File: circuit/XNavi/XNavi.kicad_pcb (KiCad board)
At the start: 2 copper layers, 60 x 60 mm, 34 parts, among them J1 Micro_SD_Card_Det, J2 Conn_01x06, J3 Conn_01x04, J4 Conn_01x06, J5 Conn_01x02, J6 Conn_Coaxial, J7 Conn_01x04, U1 STM32G441KBTx, U3 ASM330LHHTR, U4 MAX-M10S, U5 MAX3485

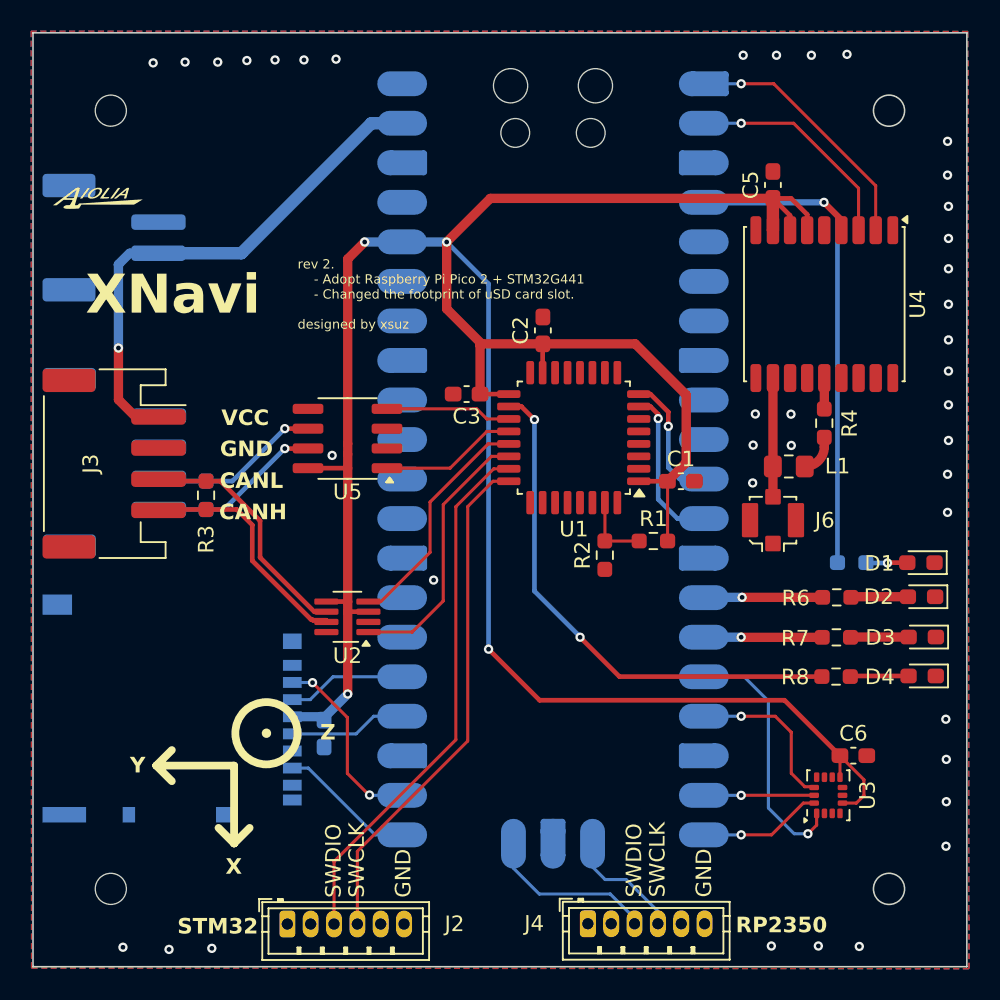
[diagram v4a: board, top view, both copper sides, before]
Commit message: UARTの信号線変更,基板を発注
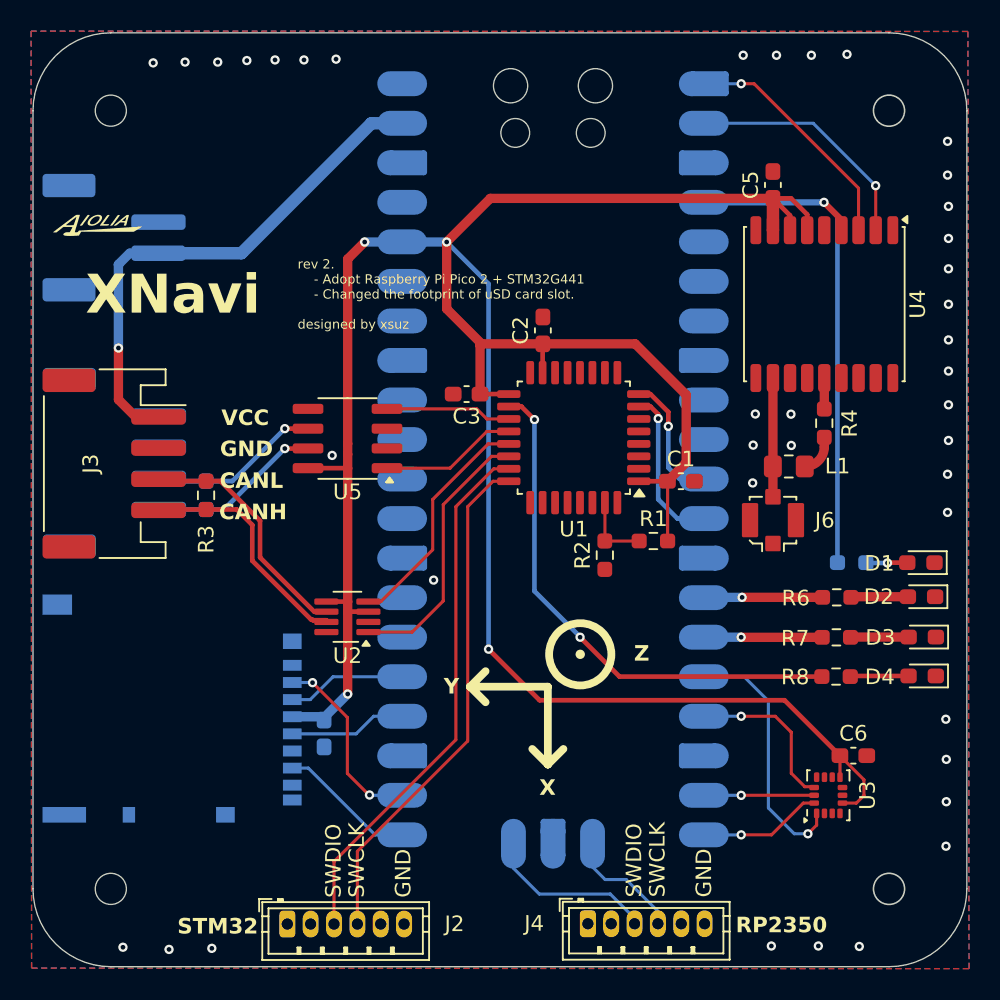
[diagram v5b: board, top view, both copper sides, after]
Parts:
- moved G*** 1.74 mm to (24.1, 32.5)
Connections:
- U4 pad 2: TX1 -> RX1
- U4 pad 3: RX1 -> TX1
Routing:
- net TX1: track 16.6 -> 15.4 mm
- net RX1: track 14.4 -> 15.6 mm
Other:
- outline, holes or cut-outs redrawn
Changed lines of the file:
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@@
 			(outputformat 1)
 			(mirror no)
-			(drillshape 1)
+			(drillshape 0)
 			(scaleselection 1)
-			(outputdirectory "")
+			(outputdirectory "out")
 		)
 	)
@@
 			(layers "F.Cu" "F.Mask" "F.Paste")
 			(roundrect_rratio 0.25)
-			(net 44 "TX1")
+			(net 35 "RX1")
 			(pinfunction "TXD")
 			(pintype "output")
@@
 			(layers "F.Cu" "F.Mask" "F.Paste")
 			(roundrect_rratio 0.25)
-			(net 35 "RX1")
+			(net 44 "TX1")
 			(pinfunction "RXD")
 			(pintype "input")
@@
 	(footprint "AIOLIA:AIOLIA"
 		(layer "F.Cu")
-		(at 24.133585 30.715897 -30)
+		(at 24.123585 32.455897 -30)
 		(property "Reference" "G***"
 			(at 0 0 150)
@@
 	)
 	(gr_circle
-		(center 35 65)
-		(end 35.25 65)
+		(center 55.16 59.93)
+		(end 55.41 59.93)
 		(stroke
 			(width 0.1)
@@
 	)
 	(gr_circle
-		(center 35 65)
-		(end 37 65)
+		(center 55.16 59.93)
+		(end 57.16 59.93)
 		(stroke
 			(width 0.5)
@@
 	)
 	(gr_line
-		(start 27.92 67.08)
-		(end 28.92 66.08)
+		(start 48.08 62.01)
+		(end 49.08 61.01)
 		(stroke
 			(width 0.5)
@@
 	)
 	(gr_line
-		(start 32.92 72.08)
-		(end 33.92 71.08)
+		(start 53.08 67.01)
+		(end 54.08 66.01)
 		(stroke
 			(width 0.5)
@@
 	)
 	(gr_line
-		(start 32.92 67.08)
-		(end 32.92 72.08)
+		(start 53.08 62.01)
+		(end 53.08 67.01)
 		(stroke
 			(width 0.5)
@@
 	)
 	(gr_line
-		(start 32.92 67.08)
-		(end 27.92 67.08)
+		(start 53.08 62.01)
+		(end 48.08 62.01)
 		(stroke
 			(width 0.5)
@@
 	)
 	(gr_line
-		(start 32.92 72.08)
-		(end 31.92 71.08)
+		(start 53.08 67.01)
+		(end 52.08 66.01)
 		(stroke
 			(width 0.5)
@@
 	)
 	(gr_line
-		(start 27.92 67.08)
-		(end 28.92 68.08)
+		(start 48.08 62.01)
+		(end 49.08 63.01)
 		(stroke
 			(width 0.5)
@@
 		(layer "Dwgs.User")
 	)
-	(gr_rect
-		(start 20 20)
-		(end 80 80)
+	(gr_arc
+		(start 25 80)
+		(mid 21.464466 78.535534)
+		(end 20 75)
 		(stroke
-			(width 0.1)
+			(width 0.05)
 			(type solid)
 		)
-		(fill no)
 		(layer "Edge.Cuts")
 	)
@@
 		(layer "Edge.Cuts")
 	)
+	(gr_line
+		(start 75 20)
+		(end 25 20)
+		(stroke
+			(width 0.05)
+			(type default)
+		)
+		(layer "Edge.Cuts")
+	)
+	(gr_line
+		(start 20 25)
+		(end 20 75)
+		(stroke
+			(width 0.05)
+			(type default)
+		)
+		(layer "Edge.Cuts")
+	)
+	(gr_line
+		(start 25 80)
+		(end 75 80)
+		(stroke
+			(width 0.05)
+			(type default)
+		)
+		(layer "Edge.Cuts")
+	)
+	(gr_arc
+		(start 20 25)
+		(mid 21.464466 21.464466)
+		(end 25 20)
+		(stroke
+			(width 0.05)
+			(type solid)
+		)
+		(layer "Edge.Cuts")
+	)
+	(gr_arc
+		(start 80 75)
+		(mid 78.535534 78.535534)
+		(end 75 80)
+		(stroke
+			(width 0.05)
+			(type solid)
+		)
+		(layer "Edge.Cuts")
+	)
+	(gr_arc
+		(start 75 20)
+		(mid 78.535534 21.464466)
+		(end 80 25)
+		(stroke
+			(width 0.05)
+			(type solid)
+		)
+		(layer "Edge.Cuts")
+	)
 	(gr_circle
 		(center 75 75)
@@
 		(layer "Edge.Cuts")
 	)
+	(gr_line
+		(start 80 75)
+		(end 80 25)
+		(stroke
+			(width 0.05)
+			(type default)
+		)
+		(layer "Edge.Cuts")
+	)
 	(gr_text "Z"
-		(at 38.45 65.53 0)
+		(at 58.61 60.46 0)
 		(layer "F.SilkS")
 		(effects
@@
 	)
 	(gr_text "Y"
-		(at 26.23 67.64 0)
+		(at 46.39 62.57 0)
 		(layer "F.SilkS")
 		(effects
@@
 	)
 	(gr_text "X"
-		(at 32.37 74.15 0)
+		(at 52.53 69.08 0)
 		(layer "F.SilkS")
 		(effects
@@
 	)
 	(segment
-		(start 73.0425 29.9825)
-		(end 68.87 25.81)
-		(width 0.2)
-		(layer "F.Cu")
-		(net 35)
-	)
-	(segment
-		(start 73.0425 32.68)
-		(end 73.0425 29.9825)
-		(width 0.2)
-		(layer "F.Cu")
-		(net 35)
-	)
-	(segment
-		(start 68.87 25.81)
-		(end 65.5 25.81)
+		(start 74.1425 32.68)
+		(end 74.1425 29.8225)
 		(width 0.2)
 		(layer "F.Cu")
@@
 	)
 	(via
-		(at 65.5 25.81)
+		(at 74.14 29.82)
 		(size 0.6)
 		(drill 0.3)
@@
 	)
 	(segment
-		(start 65.5 25.81)
+		(start 74.14 29.82)
+		(end 70.13 25.81)
+		(width 0.2)
+		(layer "B.Cu")
+		(net 35)
+	)
+	(segment
+		(start 70.13 25.81)
 		(end 63.1 25.81)
 		(width 0.2)
@@
 	)
 	(segment
-		(start 67.59 23.27)
-		(end 65.5 23.27)
+		(start 73.0425 29.9825)
+		(end 66.33 23.27)
 		(width 0.2)
 		(layer "F.Cu")
@@
 	)
 	(segment
-		(start 74.1425 32.68)
-		(end 74.1425 29.8225)
+		(start 73.0425 32.68)
+		(end 73.0425 29.9825)
 		(width 0.2)
 		(layer "F.Cu")
@@
 	)
 	(segment
-		(start 74.1425 29.8225)
-		(end 67.59 23.27)
+		(start 66.33 23.27)
+		(end 65.5 23.27)
 		(width 0.2)
 		(layer "F.Cu")
@@
 	)
 	(segment
-		(start 50.56 46.4)
+		(start 49.25 46.41)
 		(end 50.57 46.41)
 		(width 0.2)
@@
 	)
 	(segment
-		(start 49.25 46.41)
-		(end 50.57 46.41)
+		(start 42.35 56.54)
+		(end 45.68 53.21)
 		(width 0.2)
 		(layer "F.Cu")
@@
 	)
 	(segment
-		(start 45.51 53.38)
-		(end 45.51 50.15)
+		(start 41.55 56.54)
+		(end 42.35 56.54)
 		(width 0.2)
 		(layer "F.Cu")
@@
 	)
 	(segment
-		(start 45.51 50.15)
-		(end 49.25 46.41)
+		(start 50.56 46.4)
+		(end 50.57 46.41)
 		(width 0.2)
 		(layer "F.Cu")
@@
 	)
 	(segment
-		(start 42.35 56.54)
-		(end 45.51 53.38)
+		(start 45.68 53.21)
+		(end 45.68 49.98)
 		(width 0.2)
 		(layer "F.Cu")
@@
 	)
 	(segment
-		(start 41.55 56.54)
-		(end 42.35 56.54)
+		(start 45.68 49.98)
+		(end 49.25 46.41)
 		(width 0.2)
 		(layer "F.Cu")
